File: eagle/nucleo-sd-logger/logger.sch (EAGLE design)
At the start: 13 parts

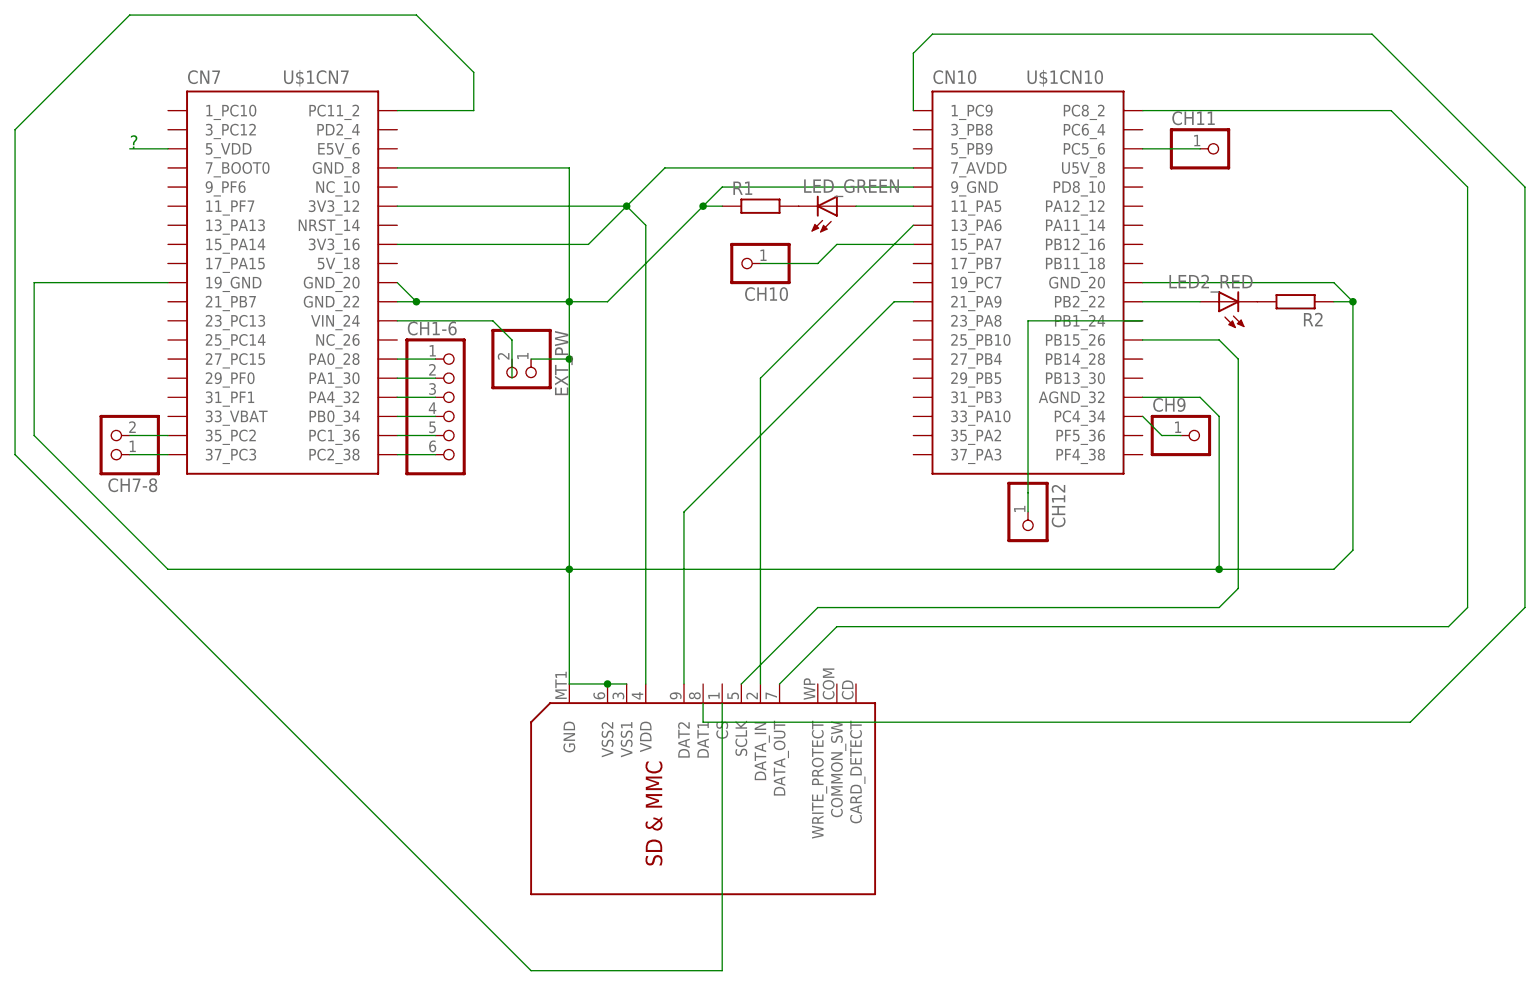
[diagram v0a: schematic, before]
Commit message: [schematic] Added SD bindings
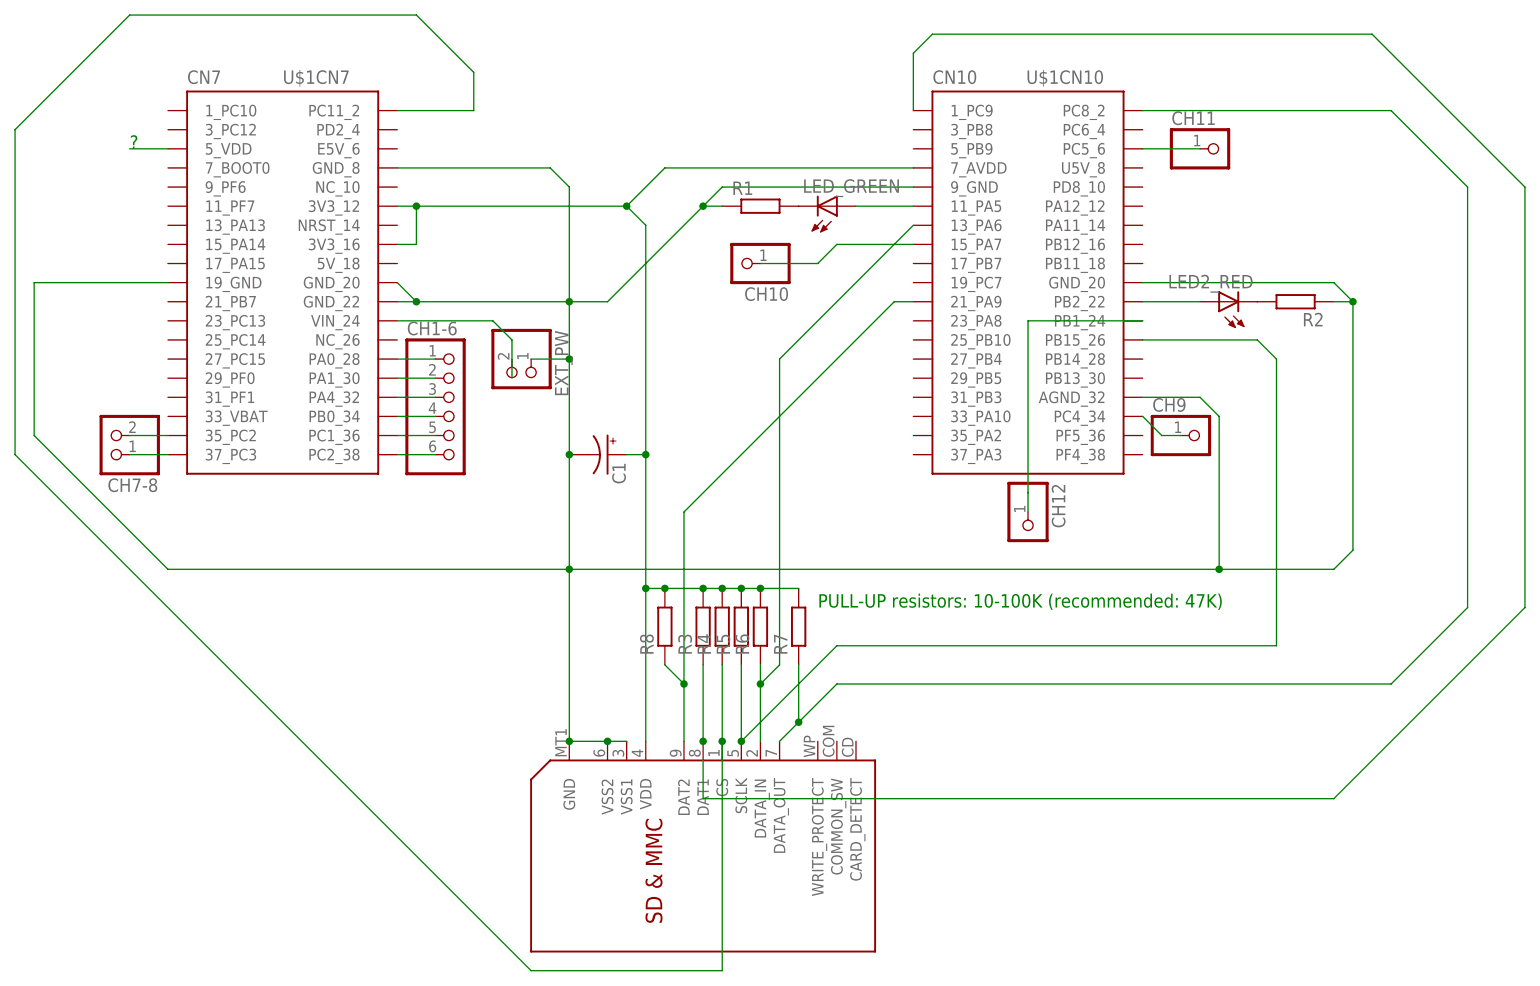
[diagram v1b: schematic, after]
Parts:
- added C1: (no value), resistor:CPOL-USE5-10.5
- added R3, R4, R5, R6, R7, R8: (no value), resistor:R-EU_M3216
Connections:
- removed net VSS1: U$2.VSS1, U$2.VSS2
- new net N$25: R3.1, U$2.DAT1
- net GND: now also C1.-, U$2.VSS1, U$2.VSS2
- net N$11: now also R5.1
- net N$3: now also R7.1
- net N$7: now also R8.1
- net N$8: now also R4.1, U$2.CS
- net N$9: now also R6.1
- net VDD: now also C1.+, R3.2, R4.2, R5.2, R6.2, R7.2, R8.2
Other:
- note added: "PULL-UP resistors: 10-100K (recommended: 47K)"

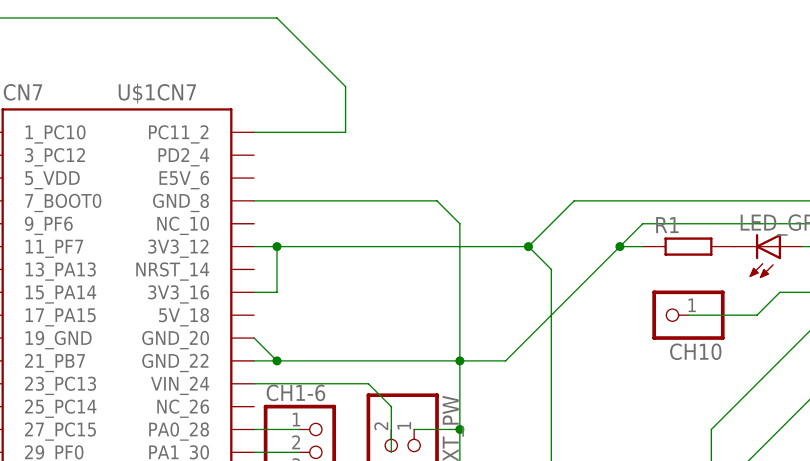
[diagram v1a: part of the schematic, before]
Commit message: Started support of "detailed mode"
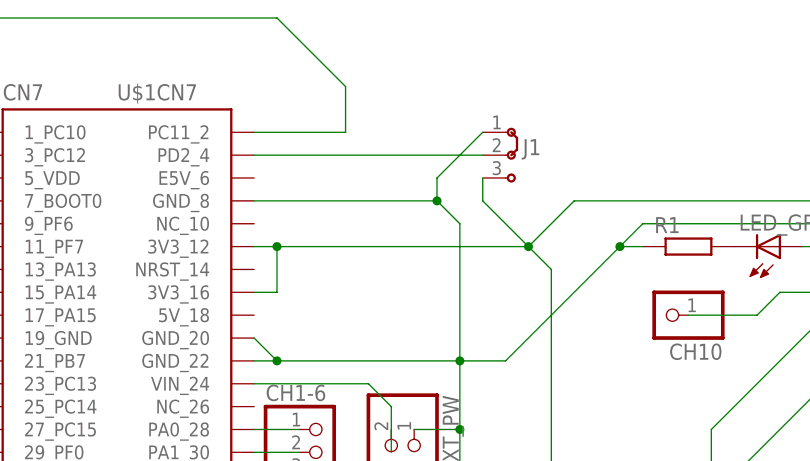
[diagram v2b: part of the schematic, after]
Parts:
- added J1: (no value), jumper:J2X2MM
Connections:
- new net N$26: J1.2, U$1CN7.PD2_4
- net GND: now also J1.1
- net VDD: now also J1.3
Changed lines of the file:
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@@
 <part name="R8" library="resistor" deviceset="R-EU_" device="M3216"/>
 <part name="C1" library="resistor" deviceset="CPOL-US" device="E5-10.5"/>
+<part name="J1" library="jumper" deviceset="J2" device="X2MM"/>
 </parts>
 <sheets>
@@
 <instance part="R8" gate="G$1" x="109.22" y="25.4" rot="R90"/>
 <instance part="C1" gate="G$1" x="101.6" y="48.26" rot="R270"/>
+<instance part="J1" gate="G$1" x="101.6" y="91.44"/>
 </instances>
 <busses>
@@
 <pinref part="C1" gate="G$1" pin="-"/>
 <junction x="96.52" y="48.26"/>
+<pinref part="J1" gate="G$1" pin="1"/>
+<wire x1="99.06" y1="93.98" x2="93.98" y2="88.9" width="0.1524" layer="91"/>
+<wire x1="93.98" y1="88.9" x2="93.98" y2="86.36" width="0.1524" layer="91"/>
+<junction x="93.98" y="86.36"/>
 </segment>
 </net>
@@
 <wire x1="104.14" y1="48.26" x2="106.68" y2="48.26" width="0.1524" layer="91"/>
 <junction x="106.68" y="48.26"/>
+<pinref part="J1" gate="G$1" pin="3"/>
+<wire x1="99.06" y1="88.9" x2="99.06" y2="86.36" width="0.1524" layer="91"/>
+<wire x1="99.06" y1="86.36" x2="104.14" y2="81.28" width="0.1524" layer="91"/>
 </segment>
 </net>
@@
 </segment>
 </net>
+<net name="N$26" class="0">
+<segment>
+<pinref part="J1" gate="G$1" pin="2"/>
+<pinref part="U$1" gate="CN7" pin="PD2_4"/>
+<wire x1="99.06" y1="91.44" x2="73.66" y2="91.44" width="0.1524" layer="91"/>
+</segment>
+</net>

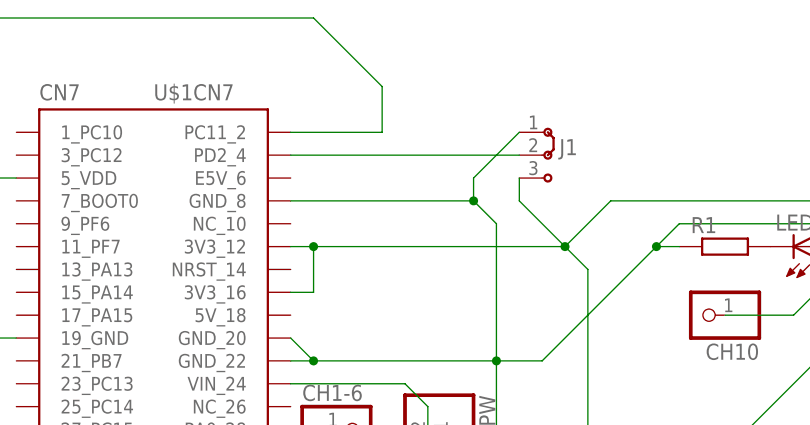
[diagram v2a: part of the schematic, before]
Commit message: Added resistor to "forceDetails" input pin
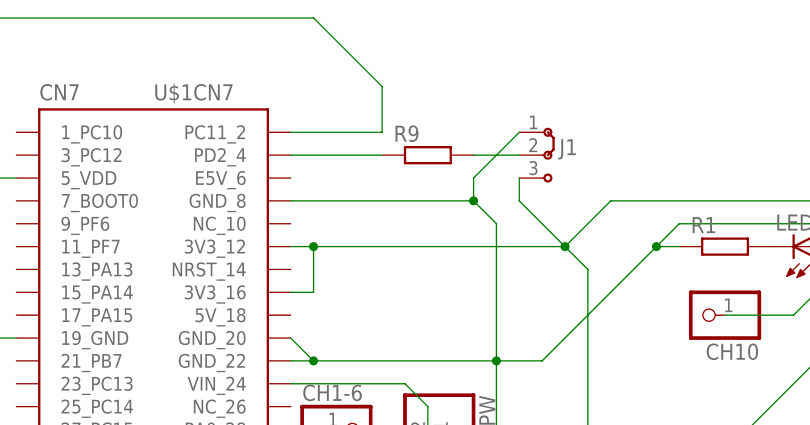
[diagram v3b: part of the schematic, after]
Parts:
- added R9: (no value), resistor:R-EU_M3216
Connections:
- new net N$27: J1.2, R9.2
- net N$26: now also R9.1; no longer J1.2
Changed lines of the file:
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@@
 <part name="C1" library="resistor" deviceset="CPOL-US" device="E5-10.5"/>
 <part name="J1" library="jumper" deviceset="J2" device="X2MM"/>
+<part name="R9" library="resistor" deviceset="R-EU_" device="M3216"/>
 </parts>
 <sheets>
@@
 <instance part="C1" gate="G$1" x="101.6" y="48.26" rot="R270"/>
 <instance part="J1" gate="G$1" x="101.6" y="91.44"/>
+<instance part="R9" gate="G$1" x="88.9" y="91.44"/>
 </instances>
 <busses>
@@
 <net name="N$26" class="0">
 <segment>
+<pinref part="U$1" gate="CN7" pin="PD2_4"/>
+<pinref part="R9" gate="G$1" pin="1"/>
+<wire x1="73.66" y1="91.44" x2="83.82" y2="91.44" width="0.1524" layer="91"/>
+</segment>
+</net>
+<net name="N$27" class="0">
+<segment>
+<pinref part="R9" gate="G$1" pin="2"/>
 <pinref part="J1" gate="G$1" pin="2"/>
-<pinref part="U$1" gate="CN7" pin="PD2_4"/>
-<wire x1="99.06" y1="91.44" x2="73.66" y2="91.44" width="0.1524" layer="91"/>
-</segment>
-</net>
+<wire x1="93.98" y1="91.44" x2="99.06" y2="91.44" width="0.1524" layer="91"/>
+</segment>
+</net>
